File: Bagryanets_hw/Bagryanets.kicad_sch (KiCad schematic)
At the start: 83 parts, among them Q1 SI2302CDS, Q2 SI2302CDS, Q3 SI2302CDS, U1 MCP1700-3302E_SOT23, U2 LMV721M5, U3 LMV721M5, X1 USBC-16P, X2 PLS-6 LOCK, X3 HU-2/WF-2 Battery, X4 HU-2/WF-2 SPST Switch

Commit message: Updated schematic
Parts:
- added C38, C39: 680p, Capacitors:CAP_0603, symbol Device:C
- added C40: 100n, Capacitors:CAP_0603, symbol Device:C
- added R15, R16: 1k, Resistors:RES_0603, symbol Device:R
- added SW1: SW_Push, symbol Switch:SW_Push
- C1, C10, C12, C13, C14, C16, C17, C19, C2, C21, C23, C24, C25, C3, C8: footprint Capacitors:CAP_0402 -> Capacitors:CAP_0603
- C5, C6: value * -> 1p*
- HA1: value HCM1201X -> HC0901A
- X3, X4: footprint Connector_PinHeader_2.54mm:PinHeader_1x02_P2.54mm_Vertical -> Connector_PinHeader_2.54mm:PinHeader_1x02_P2.54mm_Horizontal
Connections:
- net Buzzer: now also DD2.27 (PB1); no longer DD2.55 (PB3)
- net GND: now also C38.2, C39.2, C40.1, SW1.1
- net IR_IN1: now also DD2.15 (PA1), C38.1, R15.2; no longer C5.1, DD2.14 (PA0), R6.2, U2.1
- net IR_IN2: now also DD2.16 (PA2), C39.1, R16.2; no longer C6.1, DD2.15 (PA1), R7.2, U3.1
- net L.DIO0: now also DD2.25 (PC5); no longer DD2.8 (PC0)
- net L.DIO1: now also DD2.2 (PC13); no longer DD2.9 (PC1)
- net L.RESET: now also DD2.14 (PA0); no longer DD2.41 (PA8)
- net LED.B: now also DD2.37 (PC6); no longer DD2.56 (PB4)
- net LED.G: now also DD2.39 (PC8); no longer DD2.58 (PB6)
- net LED.R: now also DD2.38 (PC7); no longer DD2.57 (PB5)
- net UART_RX: now also DD2.43 (PA10); no longer DD2.17 (PA3)
- net UART_TX: now also DD2.42 (PA9); no longer DD2.16 (PA2)
- net at DD2.7 (NRST): now also C40.2, SW1.2
- net IR_O: no longer names the net of DD2.26 (PB0)
- net IR_O: no longer Q2.1 (G)
- new net: C6.1, R16.1, R7.2, U3.1
- new net: C5.1, R15.1, R6.2, U2.1
- new net IR_Out: DD2.41 (PA8), Q2.1 (G)
- no-connect marks 43 -> 42
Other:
- note added: "!!Переделать посадочное место!!"
- note added: "ADC: 1..7 - PA1..PA7 8, 9 - PB0, PB1 10..15 - PC0..PC5"
- note added: "RGB LED - 3 канала таймера TIM3: 1 - PA6/PC6 2 - PA7/PC7 3 - PB0/PC8 4 - PB1/PC9"
- note added: "SPI1: Lora SCK - PA5/PB3 MISO - PA6/PB4 MOSI - PA7/PB5 NSS - PA4/PA15"
- note added: "ST-Link: SWDIO - PA13 SWCLK - PA14"
- note added: "TIM15 - формирует частоту пачек для TIM1 - внутреннее соединение Заполнение пачек - ИК выход TIM1: 1 - PA8 2 - PA9 3 - PA10 4 - PA11"
- note added: "TIM2 - Chibi OS Или обнаружение сигнала через подсчёт отсчётов 1 - ??? 2 - PA1/PB3 3 - PA2/PB10 4 - PA3/PB11"
- note added: "USB_DM - PA11 USB_DP - PA12"
- note added: "Излучатель звука электромагнитный"
- note added: "Конденсатор рекомендуется по даташиту"
- note added: "Консоль для отладки USART1: TX - PA9/PB6 RX - PA10/PB7"
- note added: "Не важно на какой пин запихнуть"
- note added: "Перед АЦП добавлен фильтр на 250 кГц (по факту чуть меньше) Частота дискретизации 500 кГц"
- note added: "Пищалка TIM14: 1 - PA4/PA7/PB1"
- note added: "Хотелось бы просыпаться от радио по DIO0/DIO1 + добавить EXTI прерывание?? WKUP: 1 - PA0 2 - PC13 3 - PE6 - нет у данного МК 4 - PA2 5 - PC5 6 - PB5 7 - PB15"
- moved on the sheet: C10, C11, C12, C13, C14, C15, C16, C17, C18, C19, C20, C21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

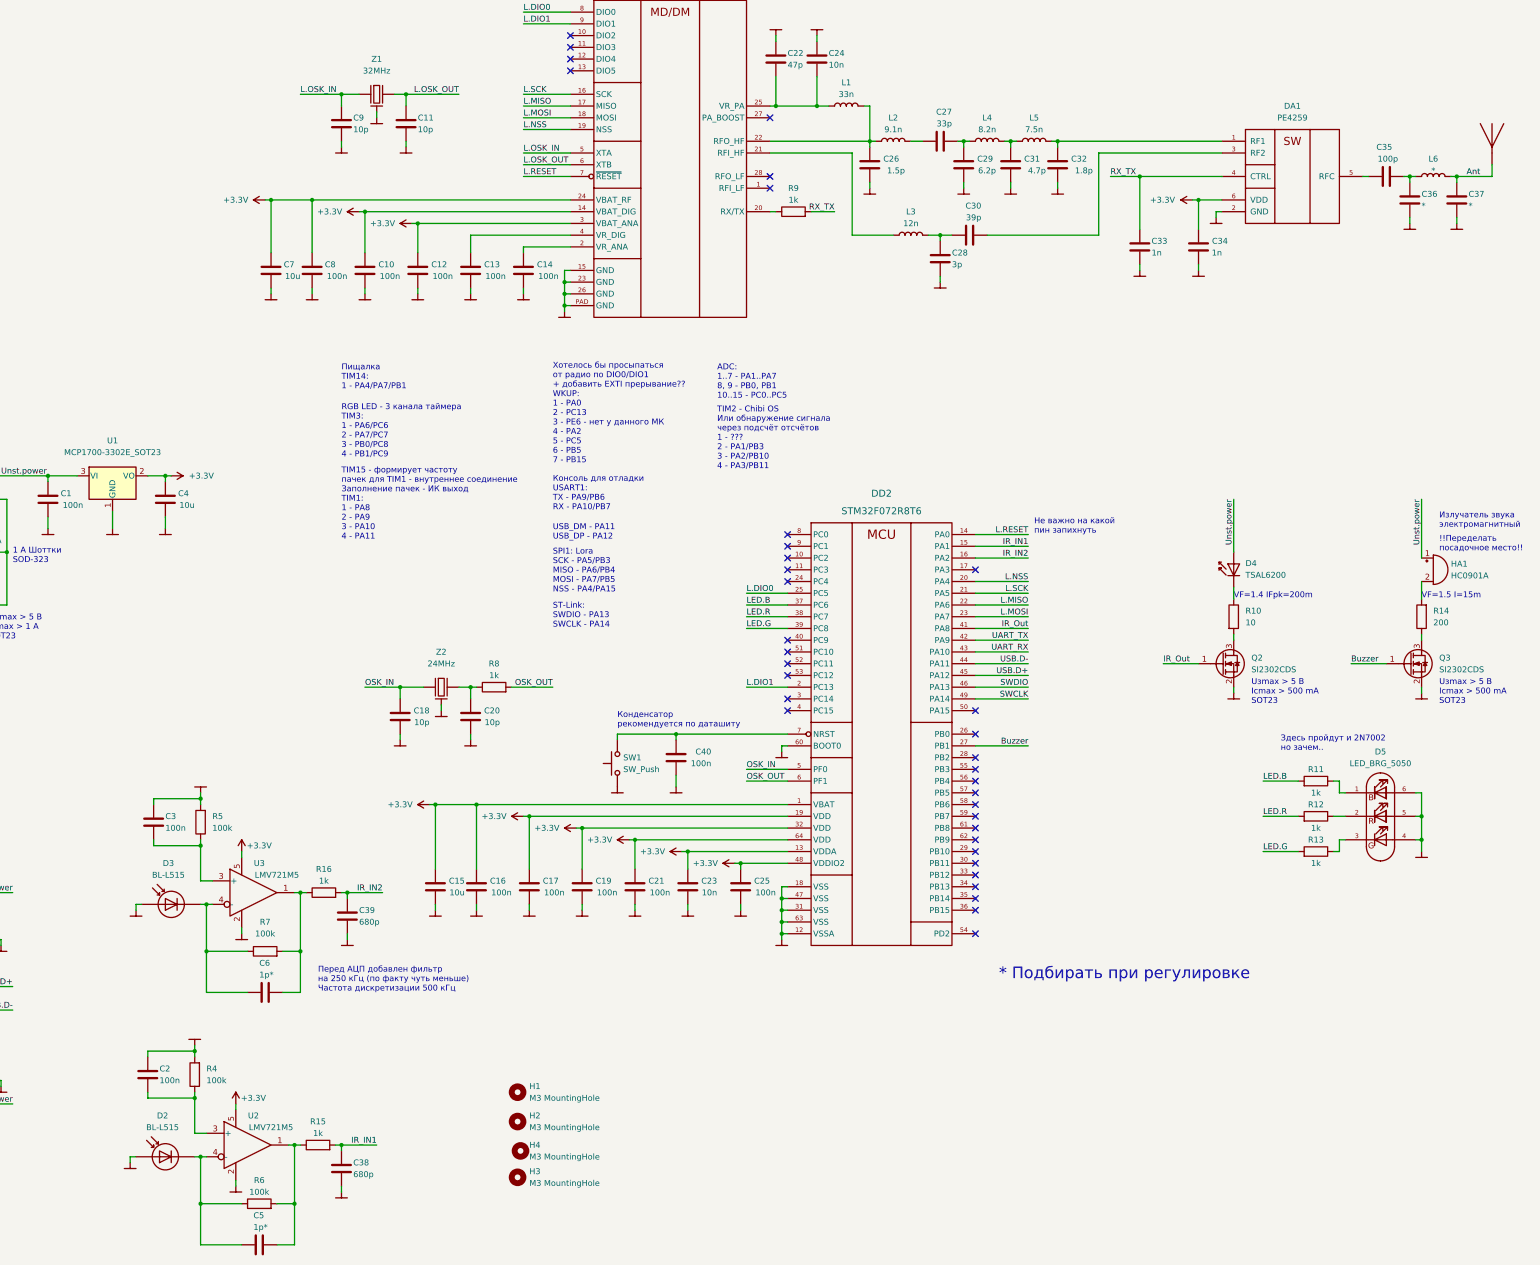
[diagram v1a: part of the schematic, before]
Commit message: Added analog power supply filter
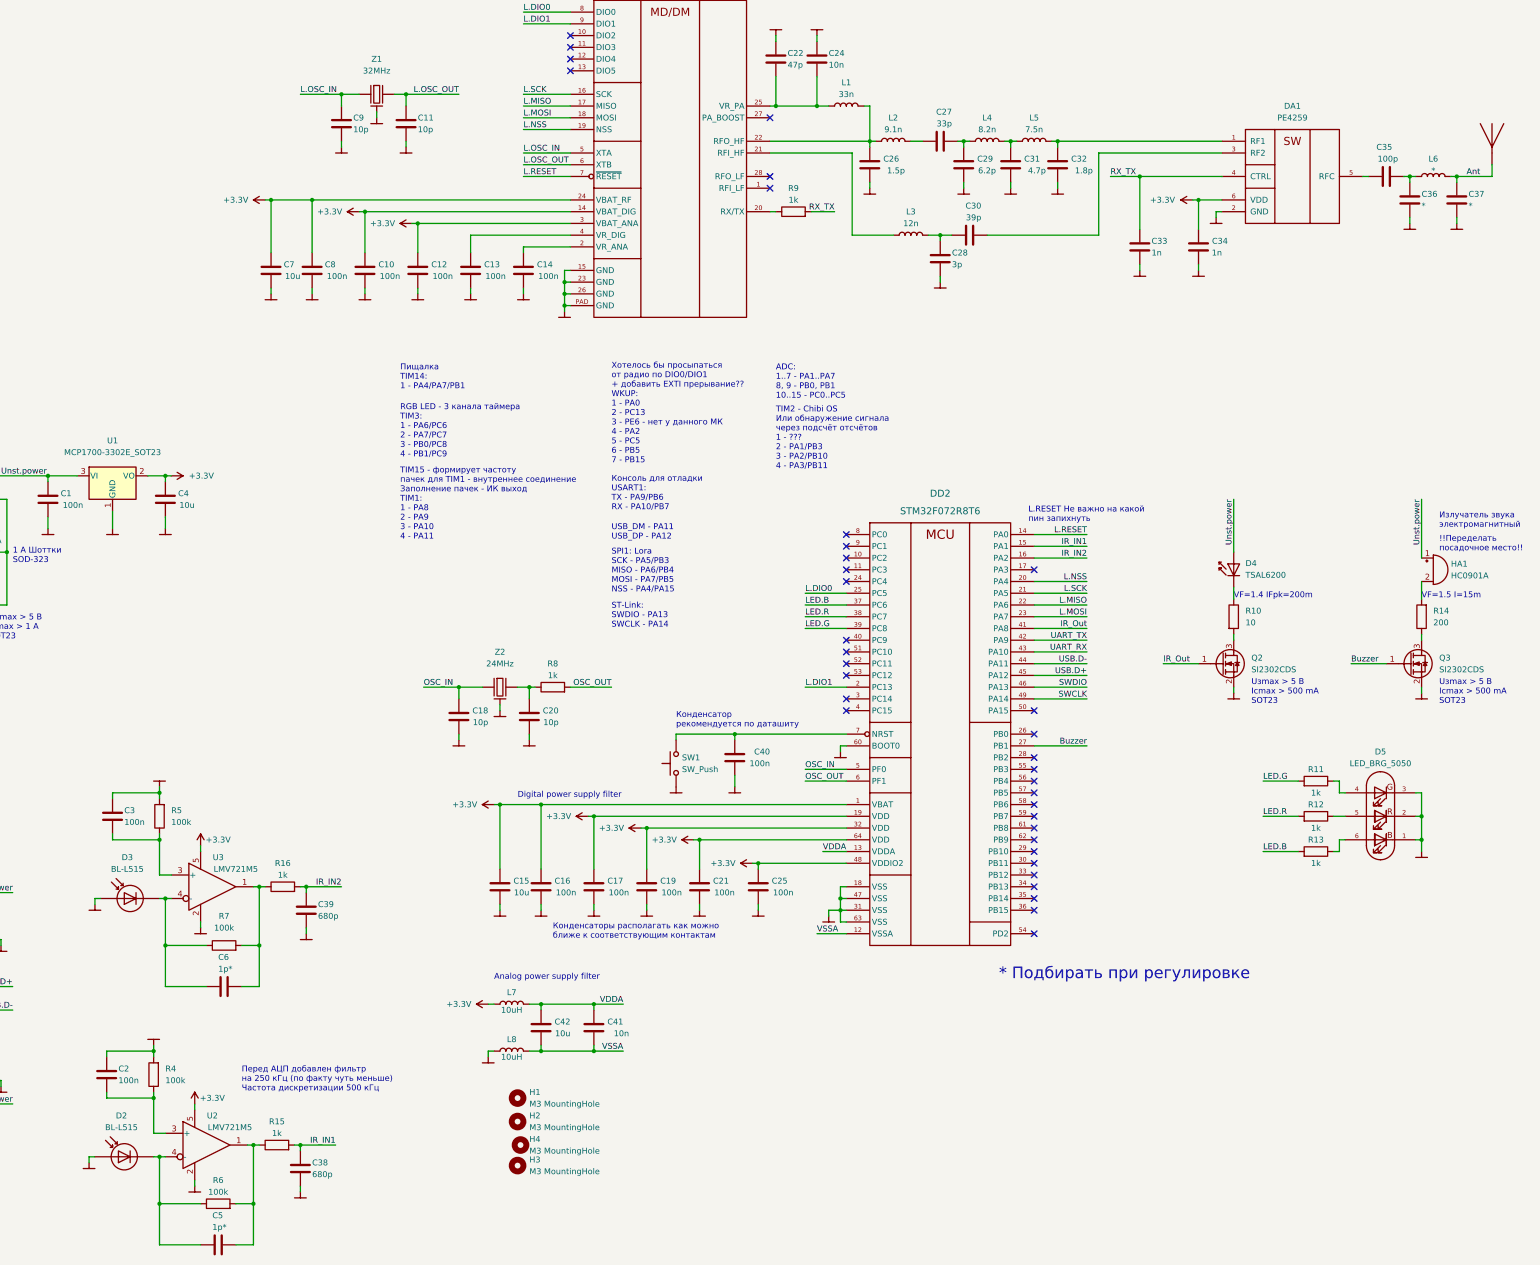
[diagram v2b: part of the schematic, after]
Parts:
- removed C23: 10n, Capacitors:CAP_0603, symbol Device:C
- added C41: 10n, Capacitors:CAP_0603, symbol Device:C
- added C42: 10u, Capacitors:CAP_0603, symbol Device:C
- added L7, L8: 10uH, Inductor_SMD:L_0805_2012Metric_Pad1.15x1.40mm_HandSolder, symbol Device:L
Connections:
- net +3V3: now also L7.1; no longer DD2.13 (VDDA)
- net GND: now also D5.1 (RK), D5.2 (GK), D5.3 (BK), L8.1; no longer D5.4 (BA), D5.5 (GA), D5.6 (RA), DD2.12 (VSSA)
- net LED.B: now also R13.2; no longer R11.2
- net LED.G: now also R11.2; no longer R13.2
- net at R11.1: now also D5.4 (BA); no longer D5.1 (RK)
- net at R12.1: now also D5.5 (GA); no longer D5.2 (GK)
- net at R13.1: now also D5.6 (RA); no longer D5.3 (BK)
- net L.OSK_IN renamed L.OSC_IN
- net L.OSK_OUT renamed L.OSC_OUT
- net OSK_IN renamed OSC_IN
- net OSK_OUT renamed OSC_OUT
- new net VDDA: C41.2, C42.2, DD2.13 (VDDA), L7.2
- new net VSSA: C41.1, C42.1, DD2.12 (VSSA), L8.2
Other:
- note added: "Analog power supply filter"
- note added: "Digital power supply filter"
- note added: "L.RESET Не важно на какой пин запихнуть"
- note added: "Конденсаторы располагать как можно ближе к соответствующим контактам"
- note removed: "Здесь пройдут и 2N7002 но зачем.."
- note removed: "Не важно на какой пин запихнуть"
- moved on the sheet: C15, C16, C17, C18, C19, C2, C20, C21, C25, C3, C38, C39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

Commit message: PCB wiring, updated casing
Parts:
- removed AE1: Antenna, symbol #USER:Antenna
- removed H1, H2, H3, H4: M3 MountingHole, MountingHole:MountingHole_3.2mm_M3, symbol Mechanical:MountingHole
- removed X4: HU-2/WF-2 SPST Switch, Connector_PinHeader_2.54mm:PinHeader_1x02_P2.54mm_Horizontal, symbol #USER:Conn_2_GOST
- added ANT1: ANT_GENERAL, Kais_Lib:Antenna_868_Bagryanets, symbol Antennas_kl:ANT_GENERAL
- added SW2: KLS7-P8.5x8.5, Kais_Lib:KLS7-P8.5x8.5, symbol Kais_Lib:KLS7-P8.5x8.5
- HA1: value HC0901A -> HC0903A; footprint Buzzer_Beeper:Buzzer_12x9.5RM7.6 -> Buzzer_Beeper:MagneticBuzzer_CUI_CST-931RP-A
- L7, L8: footprint Inductor_SMD:L_0805_2012Metric_Pad1.15x1.40mm_HandSolder -> Inductors:IND_0805
- SW1: footprint (none) -> BtnsSwitches:SW_PUSH_6mm
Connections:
- net Ant: now also ANT1.1 (RF)
- net GND: now also ANT1.2 (GND)
- net IR_IN1: now also DD2.16 (PA2); no longer DD2.15 (PA1)
- net IR_IN2: now also DD2.15 (PA1); no longer DD2.16 (PA2)
- net Unst.power: now also SW2.1, SW2.4
- net at D1.C, Q1.3 (D): now also SW2.2, SW2.5
- no-connect marks 42 -> 44
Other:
- note added: "Миниатюрная кнопка с фиксацией"
- note removed: "!!Переделать посадочное место!!"
- note removed: "SPST1"
- note removed: "SPST2"
- moved on the sheet: C1, C4, D1, Q1, R1, U1

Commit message: Added LSE clock, USB protection, battery monitoring to schematic, PCB rewiring, cover update
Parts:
- added C23, C43, C44: 100n, Capacitors:CAP_0402, symbol Device:C
- added C45, C46: 12.5p, Capacitors:CAP_0402, symbol Device:C
- added D6: ESDA5V3L, Package_TO_SOT_SMD:SOT-23, symbol Kais_Lib:ESDA5V3L
- added F1: MF-MSMF050, Fuse:Fuse_1812_4532Metric_Pad1.30x3.40mm_HandSolder, symbol Device:Fuse
- added R17, R18, R20: 100k, Resistors:RES_0603, symbol Device:R
- added R19, R21: *, Resistors:RES_0402, symbol Device:R
- added U4: USBLC6_2SC6, SOT:SOT23-6, symbol Interface_kl:USBLC6_2XX
- added Z3: 32.768kHz, Crystal:Crystal_SMD_3215-2Pin_3.2x1.5mm, symbol Tittar_kl:CRYSTAL
- C1, C10, C12, C13, C14, C16, C17, C19, C2, C21, C24, C25, C3, C38, C39, C40, C41, C8: footprint Capacitors:CAP_0603 -> Capacitors:CAP_0402
- R11, R12, R13, R8: footprint Resistors:RES_0402 -> Resistors:RES_0603
- X2: footprint Connectors:PLS-6_LOCK -> Connector_PinHeader_2.54mm:PinHeader_1x06_P2.54mm_Horizontal
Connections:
- net Battery: now also SW2.1, SW2.4, C43.2, D6.1 (IO1), R19.2; no longer X3.1
- net GND: now also C23.1, C43.1, C44.1, C45.1, C46.1, D6.2 (IO2), D6.3 (GND), R18.1, U4.2 (GND)
- net IR_IN1: now also DD2.15 (PA1); no longer DD2.16 (PA2)
- net IR_IN2: now also DD2.16 (PA2); no longer DD2.15 (PA1)
- net USB.D+: now also U4.4 (I/O2); no longer X1.A6 (DP1), X1.B6 (DP2)
- net USB.D-: now also U4.6 (I/O1); no longer X1.A7 (DN1), X1.B7 (DN2)
- net USB.power: now also C23.2, F1.2, R21.2, U4.5 (Vbus); no longer X1.A4B9 (VBUS), X1.B4A9 (VBUS)
- net Unst.power: now also D1.C, Q1.3 (D), R17.2; no longer SW2.1, SW2.4
- net at SW2.2, SW2.5: now also X3.1, R19.1; no longer D1.C, Q1.3 (D)
- net BatCtrl: now reaches DD2.26 (PB0)
- net BatCtrl: now also C44.2, R17.1, R18.2
- net OSC32_IN: now reaches DD2.3 (PC14)
- net OSC32_IN: now also C45.2, Z3.1
- net OSC32_OUT: now reaches DD2.4 (PC15)
- net OSC32_OUT: now also R20.2
- new net: C46.2, R20.1, Z3.2
- new net Conn.D+: U4.3 (I/O2), X1.A6 (DP1), X1.B6 (DP2)
- new net Conn.D-: U4.1 (I/O1), X1.A7 (DN1), X1.B7 (DN2)
- new net VBUS: F1.1, R21.1, X1.A4B9 (VBUS), X1.B4A9 (VBUS)
- no-connect marks 44 -> 41
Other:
- note added: "500 mA Предохранитель самовосстанавливающийся"
- note added: "ИК приёмник PA1, PA2 - ADC2, ADC3"
- note added: "Контроль напряжения питания PB0 - ADC8"
- note added: "Не паять"
- note added: "Питание от 3хАА батареек и ESD защита"
- moved on the sheet: C1, C2, C3, C38, C39, C4, C41, C42, C5, C6, D1, D2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

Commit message: GOST designators
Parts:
- R14: renamed from R20; value 100k -> 1k
- renumbered C44 to C1, C6 to C10, C5 to C11, C9 to C12, C10 to C13, C11 to C14, C39 to C15, C38 to C16, C12 to C17, C45 to C18, C18 to C19, C23 to C2, C13 to C20, C15 to C21, C14 to C22, C46 to C23, C20 to C24, C16 to C25, C17 to C26, C42 to C27, C19 to C28, C41 to C29, C1 to C3, C21 to C30, C40 to C31, C25 to C32, C22 to C33, C24 to C34, C26 to C35, C27 to C36, C28 to C37, C29 to C38, C30 to C39, C43 to C4, C31 to C40, C32 to C41, C33 to C42, C34 to C43, C35 to C44, C36 to C45, C37 to C46, C4 to C5, C3 to C6, C2 to C7, C7 to C8, C8 to C9, U1 to DA1, U3 to DA2, U2 to DA3, DA1 to DA4, DD2 to DD1, L7 to L1, L8 to L2, L1 to L3, L2 to L4, L3 to L5, L4 to L6, L5 to L7, L6 to L8, R7 to R10, R6 to R11, R16 to R12, R15 to R13, R8 to R15, R9 to R16, R10 to R17, R11 to R18, R12 to R19, R17 to R2, R13 to R20, R14 to R21, R18 to R3, R2 to R4, R3 to R5, R21 to R6, R19 to R7, R5 to R8, R4 to R9, SW2 to SB1, SW1 to SB2, DD1 to U1, D1 to VD1, U4 to VD2, D6 to VD3, D3 to VD4, D2 to VD5, D4 to VD6, D5 to VD7, Q1 to VT1, Q2 to VT2, Q3 to VT3, ANT1 to WA1, X2 to XP1, X3 to XP2, X1 to XS1, Z1 to ZQ1, Z3 to ZQ2, Z2 to ZQ3
